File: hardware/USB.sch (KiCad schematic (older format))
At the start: 8 parts, among them J6 USB_B_Micro, U3 MIC5504-3.3YM5

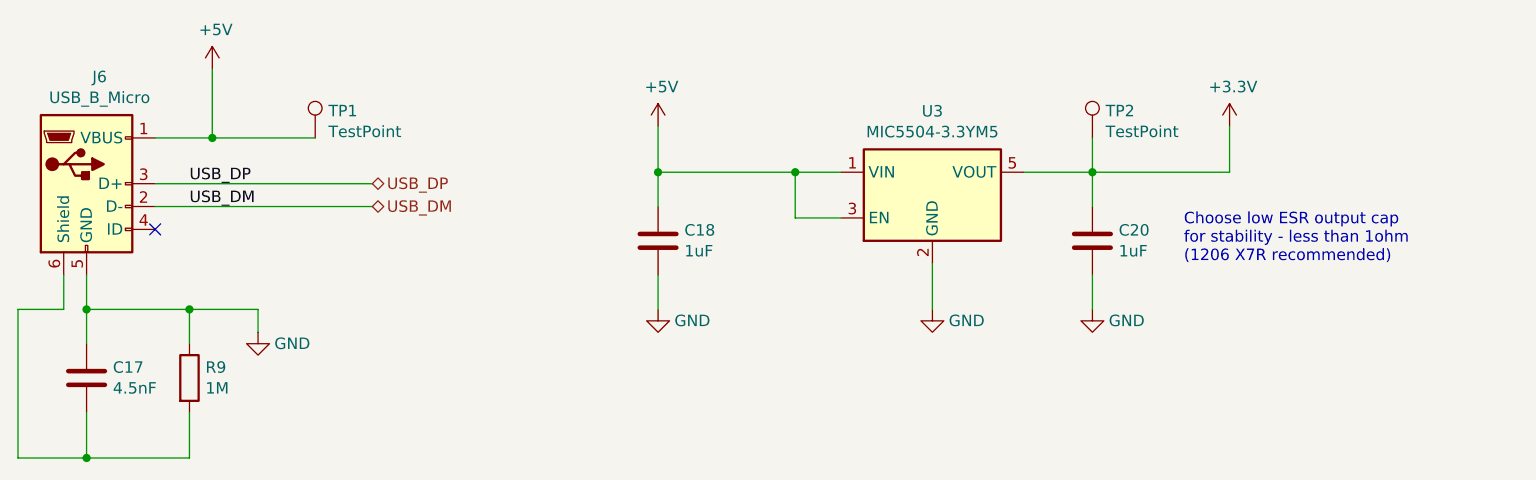
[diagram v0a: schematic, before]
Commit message: Moved all Kicad stuff to /hardware/ directory
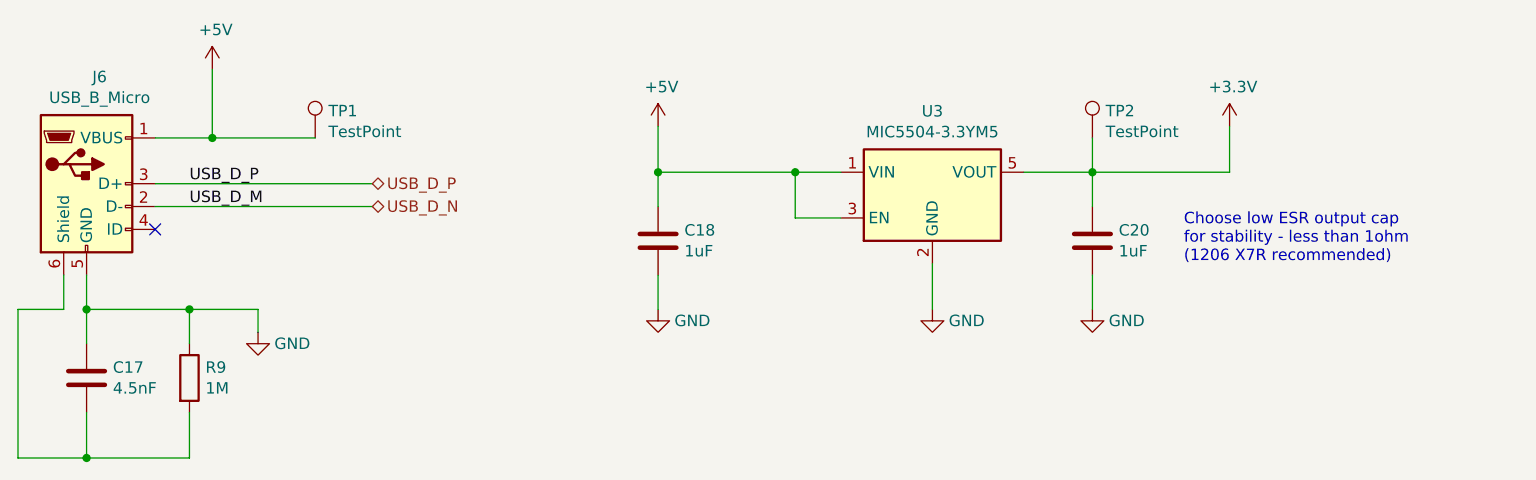
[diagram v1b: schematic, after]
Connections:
- net USB_DM renamed USB_D_N
- net USB_DP renamed USB_D_P
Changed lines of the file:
@@
 	3150 3950 3150 3800
 Text Label 3700 3500 0    50   ~ 0
-USB_DM
+USB_D_M
 Text Label 3700 3400 0    50   ~ 0
-USB_DP
+USB_D_P
 Wire Wire Line
 	3550 3200 3800 3200
@@
 	7650 3350 7650 3200
 Text HLabel 4500 3400 2    50   BiDi ~ 0
-USB_DP
+USB_D_P
 Text HLabel 4500 3500 2    50   BiDi ~ 0
-USB_DM
+USB_D_N
 Wire Wire Line
 	3550 3500 4500 3500
